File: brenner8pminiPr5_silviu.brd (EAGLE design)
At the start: 82.5 x 43 mm, 39 parts, among them IC1 PIC18F2550SP, Q1 20 MHz, Q2 BC338-25, Q3 BC338-25, Q4 BC328-25, Q5 BC328-25, Q6 BF959, X2 USB-B-H

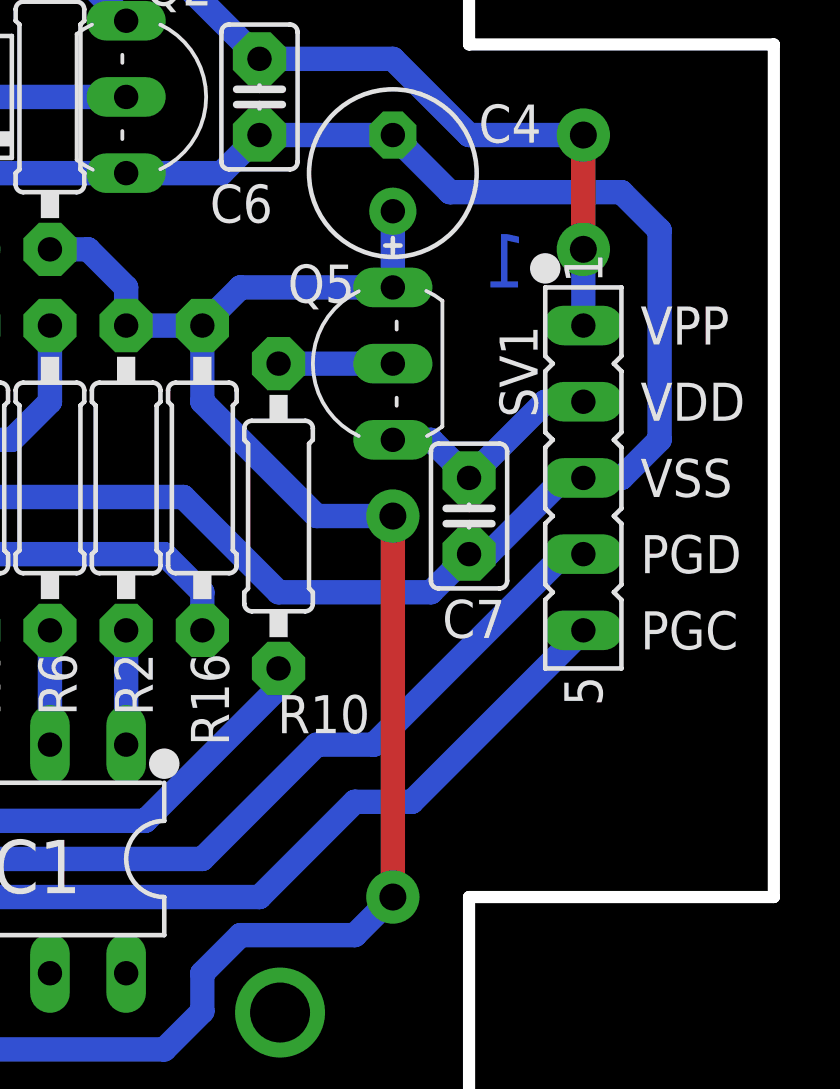
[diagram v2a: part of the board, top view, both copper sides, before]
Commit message: Header drill size set to 1mm
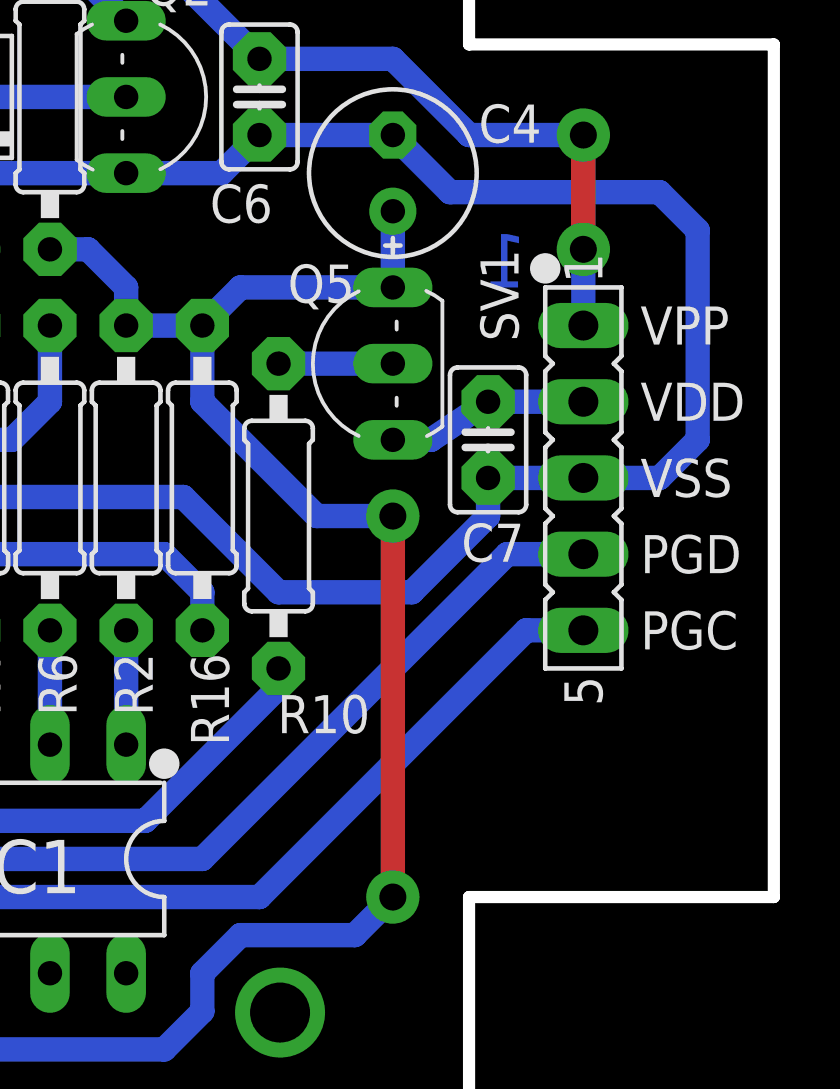
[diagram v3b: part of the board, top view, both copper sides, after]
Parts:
- moved C7 2.62 mm to (73.0, 21.6)
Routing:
- net VSS: track 210.1 -> 213.3 mm
- net N$17: track 7.93 -> 6.73 mm
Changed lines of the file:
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@@
 </element>
 <element name="SV1" library="con-lsta" package="FE05-1" value="ICSP" x="76.2" y="20.32" smashed="yes" rot="R270">
-<attribute name="NAME" x="73.406" y="25.4" size="1.27" layer="25" ratio="10" rot="R270"/>
+<attribute name="NAME" x="72.771" y="27.94" size="1.27" layer="25" ratio="10" rot="R270"/>
 <attribute name="VALUE" x="77.851" y="20.32" size="1.27" layer="27" ratio="10" rot="R270"/>
 </element>
@@
 <attribute name="VALUE" x="66.675" y="16.7894" size="1.27" layer="27" ratio="10" rot="R90"/>
 </element>
-<element name="C7" library="rcl" package="C025-025X050" value="100nF" x="72.39" y="19.05" smashed="yes" rot="R270">
-<attribute name="NAME" x="71.501" y="14.986" size="1.27" layer="25" ratio="10"/>
-<attribute name="VALUE" x="72.136" y="16.129" size="1.27" layer="27" ratio="10" rot="R270"/>
+<element name="C7" library="rcl" package="C025-025X050" value="100nF" x="73.025" y="21.59" smashed="yes" rot="R270">
+<attribute name="NAME" x="72.136" y="17.526" size="1.27" layer="25" ratio="10"/>
+<attribute name="VALUE" x="72.771" y="18.669" size="1.27" layer="27" ratio="10" rot="R270"/>
 </element>
 <element name="R11" library="rcl" package="0207/10" value="10k" x="48.26" y="20.955" smashed="yes" rot="R90">
@@
 <wire x1="53.34" y1="5.08" x2="54.61" y2="6.35" width="0.8128" layer="16"/>
 <wire x1="54.61" y1="6.35" x2="65.405" y2="6.35" width="0.8128" layer="16"/>
-<wire x1="65.405" y1="6.35" x2="68.58" y2="9.525" width="0.8128" layer="16"/>
-<wire x1="68.58" y1="9.525" x2="70.485" y2="9.525" width="0.8128" layer="16"/>
-<wire x1="70.485" y1="9.525" x2="76.2" y2="15.24" width="0.8128" layer="16"/>
+<wire x1="65.405" y1="6.35" x2="74.295" y2="15.24" width="0.8128" layer="16"/>
+<wire x1="74.295" y1="15.24" x2="76.2" y2="15.24" width="0.8128" layer="16"/>
 </signal>
 <signal name="DATA_18">
 <contactref element="IC1" pad="24"/>
 <contactref element="SV1" pad="4"/>
-<wire x1="75.565" y1="17.78" x2="76.2" y2="17.78" width="0.8128" layer="16"/>
-<wire x1="63.5" y1="7.62" x2="67.31" y2="11.43" width="0.8128" layer="16"/>
-<wire x1="67.31" y1="11.43" x2="69.215" y2="11.43" width="0.8128" layer="16"/>
-<wire x1="69.215" y1="11.43" x2="75.565" y2="17.78" width="0.8128" layer="16"/>
+<wire x1="73.66" y1="17.78" x2="76.2" y2="17.78" width="0.8128" layer="16"/>
+<wire x1="63.5" y1="7.62" x2="73.66" y2="17.78" width="0.8128" layer="16"/>
 <wire x1="53.34" y1="7.62" x2="63.5" y2="7.62" width="0.8128" layer="16"/>
 <wire x1="50.8" y1="5.08" x2="53.34" y2="7.62" width="0.8128" layer="16"/>
@@
 <contactref element="C7" pad="1"/>
 <wire x1="69.85" y1="21.59" x2="71.12" y2="21.59" width="0.8128" layer="16"/>
-<wire x1="71.12" y1="21.59" x2="72.39" y2="20.32" width="0.8128" layer="16"/>
-<wire x1="72.39" y1="20.32" x2="74.93" y2="22.86" width="0.8128" layer="16"/>
-<wire x1="74.93" y1="22.86" x2="76.2" y2="22.86" width="0.8128" layer="16"/>
+<wire x1="71.12" y1="21.59" x2="73.025" y2="22.86" width="0.8128" layer="16"/>
+<wire x1="73.025" y1="22.86" x2="76.2" y2="22.86" width="0.8128" layer="16"/>
 </signal>
 <signal name="N$19">
@@
 <wire x1="65.405" y1="31.75" x2="64.135" y2="30.48" width="0.8128" layer="16"/>
 <wire x1="60.96" y1="30.48" x2="54.61" y2="30.48" width="0.8128" layer="16"/>
-<wire x1="76.2" y1="20.32" x2="77.47" y2="20.32" width="0.8128" layer="16"/>
-<wire x1="77.47" y1="20.32" x2="78.74" y2="21.59" width="0.8128" layer="16"/>
-<wire x1="78.74" y1="21.59" x2="78.74" y2="28.575" width="0.8128" layer="16"/>
-<wire x1="78.74" y1="28.575" x2="77.47" y2="29.845" width="0.8128" layer="16"/>
+<wire x1="76.2" y1="20.32" x2="78.74" y2="20.32" width="0.8128" layer="16"/>
+<wire x1="78.74" y1="20.32" x2="80.01" y2="21.59" width="0.8128" layer="16"/>
+<wire x1="80.01" y1="21.59" x2="80.01" y2="28.575" width="0.8128" layer="16"/>
+<wire x1="80.01" y1="28.575" x2="78.74" y2="29.845" width="0.8128" layer="16"/>
 <wire x1="71.755" y1="29.845" x2="69.85" y2="31.75" width="0.8128" layer="16"/>
 <wire x1="62.865" y1="19.685" x2="66.04" y2="16.51" width="0.8128" layer="16"/>
-<wire x1="66.04" y1="16.51" x2="71.12" y2="16.51" width="0.8128" layer="16"/>
+<wire x1="66.04" y1="16.51" x2="70.485" y2="16.51" width="0.8128" layer="16"/>
 <wire x1="43.18" y1="13.97" x2="43.18" y2="11.43" width="0.8128" layer="16"/>
 <wire x1="43.815" y1="16.51" x2="43.18" y2="15.875" width="0.8128" layer="16"/>
 <wire x1="43.18" y1="15.875" x2="43.18" y2="13.97" width="0.8128" layer="16"/>
-<wire x1="77.47" y1="29.845" x2="71.755" y2="29.845" width="0.8128" layer="16"/>
+<wire x1="78.74" y1="29.845" x2="71.755" y2="29.845" width="0.8128" layer="16"/>
 <wire x1="27.94" y1="19.05" x2="31.115" y2="19.05" width="0.8128" layer="16"/>
 <wire x1="15.24" y1="30.48" x2="20.32" y2="30.48" width="0.8128" layer="16"/>
@@
 <wire x1="21.59" y1="22.86" x2="22.86" y2="22.86" width="0.8128" layer="16"/>
 <wire x1="22.86" y1="22.86" x2="25.4" y2="22.86" width="0.8128" layer="16"/>
-<wire x1="71.12" y1="16.51" x2="72.39" y2="17.78" width="0.8128" layer="16"/>
+<wire x1="70.485" y1="16.51" x2="73.025" y2="19.05" width="0.8128" layer="16"/>
+<wire x1="73.025" y1="19.05" x2="73.025" y2="20.32" width="0.8128" layer="16"/>
 <wire x1="36.195" y1="24.13" x2="38.735" y2="24.13" width="0.8128" layer="16"/>
 <wire x1="31.115" y1="19.05" x2="36.195" y2="24.13" width="0.8128" layer="16"/>
@@
 <wire x1="21.59" y1="31.75" x2="20.32" y2="30.48" width="0.8128" layer="16"/>
 <wire x1="21.59" y1="29.21" x2="20.32" y2="30.48" width="0.8128" layer="16"/>
-<wire x1="72.39" y1="17.78" x2="73.025" y2="17.78" width="0.8128" layer="16"/>
-<wire x1="73.025" y1="17.78" x2="75.565" y2="20.32" width="0.8128" layer="16"/>
-<wire x1="75.565" y1="20.32" x2="76.2" y2="20.32" width="0.8128" layer="16"/>
+<wire x1="73.025" y1="20.32" x2="76.2" y2="20.32" width="0.8128" layer="16"/>
 <wire x1="43.18" y1="19.685" x2="43.815" y2="19.05" width="0.8128" layer="16"/>
 <wire x1="43.815" y1="19.05" x2="44.45" y2="19.685" width="0.8128" layer="16"/>
